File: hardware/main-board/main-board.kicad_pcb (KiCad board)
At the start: 4 copper layers, 100 x 100 mm, 154 parts, among them J1 BOOT, J10 8P8CDouble, J11 Qwiic, J12 Qwiic, J13 Qwiic, J14 Micro_SD_Card_Det, J15 Interrupts1, J16 Interrupts2, J17 Battery, J2 USB Header, J3 JTAG, J4 5V Input, J5 StatusPanel, J6 Qwiic, J7 8P8CDouble, J8 8P8CDouble, J9 8P8CDouble, Q1 N Channel, Q10 N Channel, Q11 N Channel, Q12 N Channel, Q13 P Channel, Q14 P Channel, Q15 P Channel, Q16 P Channel, Q17 P Channel, Q2 N Channel, Q3 N Channel, Q4 N Channel, Q5 P Channel, Q6 P Channel, Q7 P Channel, Q8 P Channel, Q9 N Channel, U1 STM32H743ZITx, U10 ISL83490, U11 ISL83490, U12 ISL83490, U2 USBLC6-2SC6, U3 3.3V Reg, U4 AP2120N-3.3TRG1 / XC6206P332MR, U5 ISL83490, U6 ISL83490, U7 ISL83490, U8 ISL83490, U9 ISL83490, X1 20MHz Oscillator, X2 32.768kHz Oscillator

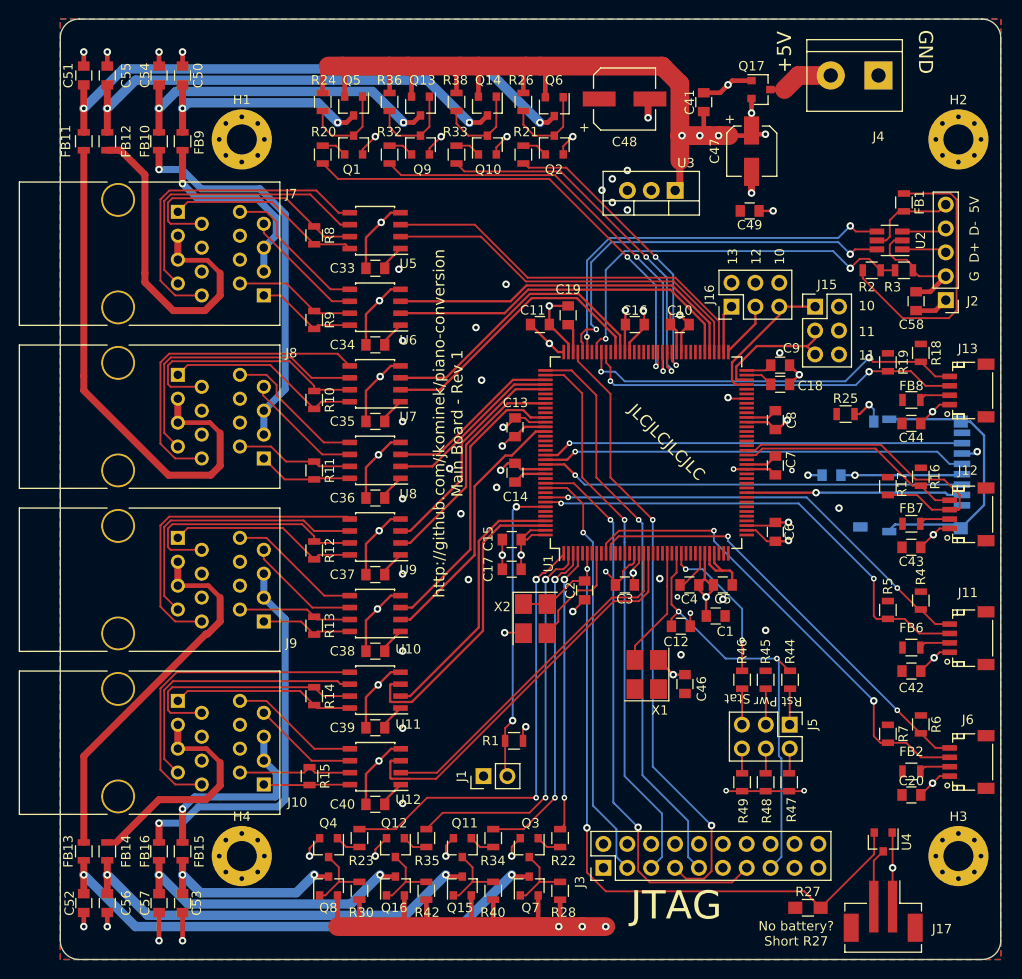
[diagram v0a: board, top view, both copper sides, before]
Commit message: main board changes for rev 2 per issue #41
* Added a bit more thermal relief to everything on the top layer
* Looked at the RS485 and I2C caps thermal relief and called it good enough.
* Fixed silkscreen of C20 and most everything else, as I upgraded to KiCad 6 footprints and the refs all moved.
* Changed the ferrite bead footprint to the handsoldering one.
* Tweaked the specified values for the Pwr and Stat LEDs, but not much.
* Removed battery connector and associated bits.
* That left remove to move over the JTAG header.
* Switched to using the SDMMC peripheral for accessing the SD card.
* Had SDCARD_DET net attached to the wrong side of the pull up; fixed.
* Made all of the high speed traces nice and filleted.
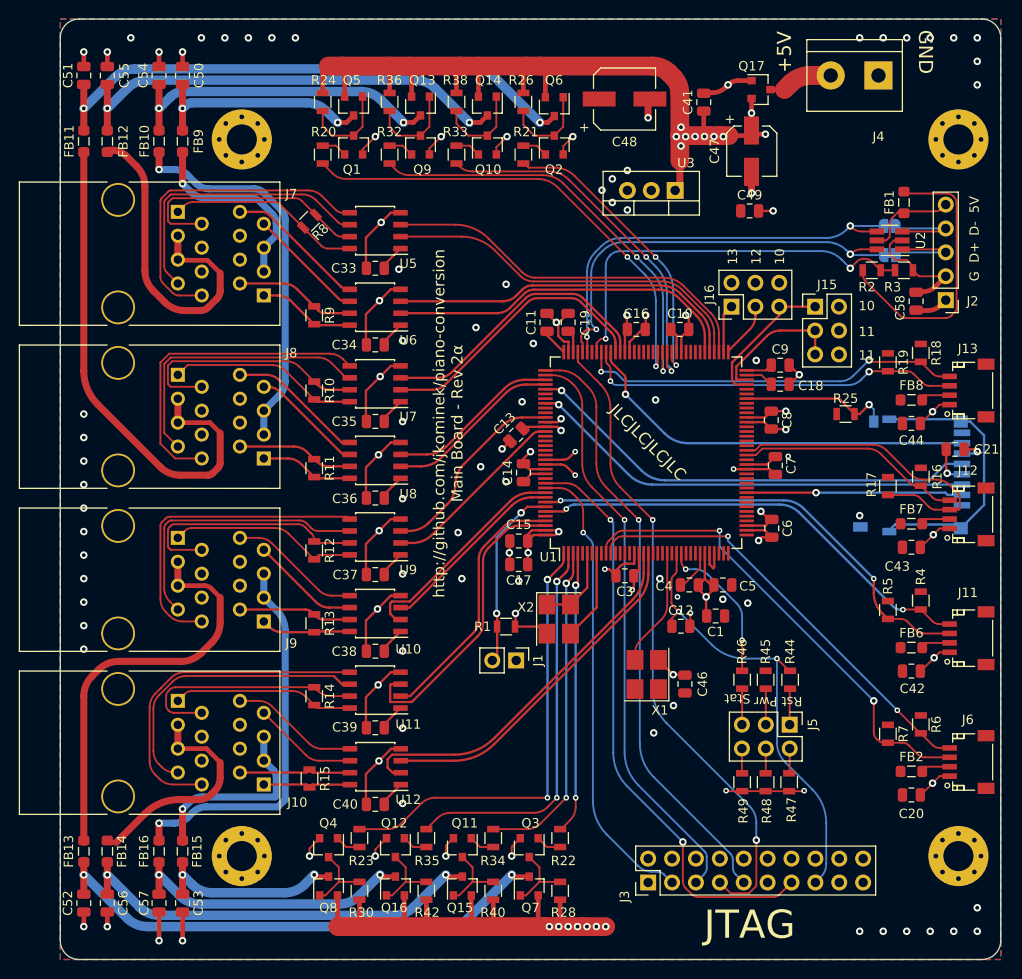
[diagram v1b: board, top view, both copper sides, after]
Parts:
- removed C2: DC6, Capacitors_SMD:C_0805
- removed J17: Battery, Connectors_JST:JST_PH_B2B-PH-SM4-TB_02x2.00mm_Straight
- removed R27: DNP, Resistors_SMD:R_0805_HandSoldering
- removed U4: AP2120N-3.3TRG1 / XC6206P332MR, TO_SOT_Packages_SMD:SOT-23
- added JP1: SolderJumper_2_Bridged, Jumper:SolderJumper-2_P1.3mm_Bridged_RoundedPad1.0x1.5mm, B.Cu at (183.2, 60.0)
- added JP2: SolderJumper_2_Bridged, Jumper:SolderJumper-2_P1.3mm_Bridged_RoundedPad1.0x1.5mm, B.Cu at (183.2, 63.1)
- C1, C10, C11, C12, C13, C14, C15, C16, C17, C18, C19, C20, C3, C33, C34, C35, C36, C37, C38, C39, C4, C40, C41, C42, C43, C44, C46, C49, C5, C50, C51, C52, C53, C54, C55, C56, C57, C58, C6, C7, C8, C9: footprint Capacitors_SMD:C_0805 -> Capacitor_SMD:C_0805_2012Metric
- C21: footprint Capacitors_SMD:C_0805 -> Capacitor_SMD:C_0805_2012Metric; moved to F.Cu
- FB1, FB10, FB11, FB12, FB13, FB14, FB15, FB16, FB2, FB6, FB7, FB8, FB9: footprint Inductors_SMD:L_0805 -> Inductor_SMD:L_0805_2012Metric_Pad1.05x1.20mm_HandSolder
- R48, R49: value 3300 -> 660
- moved C21 13.4 mm to (190.2, 83.8), turned to 180 degrees
- moved J1 12.8 mm to (143.5, 106.2), turned to -90 degrees
- moved R1 12.2 mm to (142.4, 102.6)
- moved J3 5.01 mm to (157.5, 129.8)
- moved X2 2.50 mm to (148.0, 101.8)
- moved R8 1.58 mm to (121.5, 59.5), turned to -135 degrees
- moved R10 1.00 mm to (122.0, 77.5)
- moved C3 0.97 mm to (155.0, 97.2)
- moved C17 0.90 mm to (143.8, 96.0)
- moved C14 0.90 mm to (144.2, 86.2)
- moved C13 0.82 mm to (143.5, 82.2), turned to -135 degrees
- moved C11 0.79 mm to (146.8, 70.2), turned to 90 degrees
- moved C15 0.77 mm to (143.8, 93.5)
- moved C19 0.75 mm to (149.0, 70.2)
- moved C6 0.54 mm to (170.7, 92.2)
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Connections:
- J14 pad 1: (no net) -> unconnected-(J14-Pad1)
- J14 pad 11: Net-(J14-Pad11) -> unconnected-(J14-Pad11)
- J14 pad 3: /SPI6_MOSI -> /SDMMC1_CMD
- J14 pad 5: /SPI6_SCK -> /SDMMC1_CK
- J14 pad 7: /SPI6_MISO -> /SDMMC1_D0
- J14 pad 8: (no net) -> unconnected-(J14-Pad8)
- J14 pad 9: Net-(J14-Pad9) -> /SDCARD_DET
- J3 pad 11: (no net) -> unconnected-(J3-Pad11)
- J3 pad 17: (no net) -> unconnected-(J3-Pad17)
- J3 pad 19: (no net) -> unconnected-(J3-Pad19)
- R25 pad 2: Net-(J14-Pad9) -> /SDCARD_DET
- U1 pad 102: (no net) -> unconnected-(U1-Pad102)
- U1 pad 113: /UART5_TX -> /SDMMC1_CK
- U1 pad 114: (no net) -> unconnected-(U1-Pad114)
- U1 pad 115: (no net) -> unconnected-(U1-Pad115)
- U1 pad 116: /UART5_RX -> /SDMMC1_CMD
- U1 pad 117: (no net) -> unconnected-(U1-Pad117)
- U1 pad 118: (no net) -> unconnected-(U1-Pad118)
- U1 pad 12: (no net) -> unconnected-(U1-Pad12)
- U1 pad 123: (no net) -> unconnected-(U1-Pad123)
- U1 pad 124: (no net) -> unconnected-(U1-Pad124)
- U1 pad 125: (no net) -> unconnected-(U1-Pad125)
- U1 pad 126: (no net) -> unconnected-(U1-Pad126)
- U1 pad 127: /SPI6_MISO -> unconnected-(U1-Pad127)
- U1 pad 128: /SPI6_SCK -> unconnected-(U1-Pad128)
- U1 pad 129: /SPI6_MOSI -> unconnected-(U1-Pad129)
- U1 pad 13: (no net) -> unconnected-(U1-Pad13)
- U1 pad 132: (no net) -> unconnected-(U1-Pad132)
- U1 pad 135: (no net) -> /UART5_RX
- U1 pad 136: /I2C1_SCL -> /UART5_TX
- U1 pad 139: (no net) -> /I2C1_SCL
- U1 pad 14: (no net) -> unconnected-(U1-Pad14)
- U1 pad 140: (no net) -> unconnected-(U1-Pad140)
- U1 pad 15: (no net) -> unconnected-(U1-Pad15)
- U1 pad 20: (no net) -> unconnected-(U1-Pad20)
- U1 pad 21: (no net) -> unconnected-(U1-Pad21)
- U1 pad 22: (no net) -> unconnected-(U1-Pad22)
- U1 pad 24: (no net) -> unconnected-(U1-Pad24)
- U1 pad 27: (no net) -> unconnected-(U1-Pad27)
- U1 pad 28: (no net) -> unconnected-(U1-Pad28)
- U1 pad 29: (no net) -> unconnected-(U1-Pad29)
- U1 pad 34: (no net) -> unconnected-(U1-Pad34)
- U1 pad 35: (no net) -> unconnected-(U1-Pad35)
- U1 pad 36: (no net) -> unconnected-(U1-Pad36)
- U1 pad 37: (no net) -> unconnected-(U1-Pad37)
- U1 pad 40: (no net) -> unconnected-(U1-Pad40)
- U1 pad 41: (no net) -> unconnected-(U1-Pad41)
- U1 pad 42: (no net) -> unconnected-(U1-Pad42)
- U1 pad 43: (no net) -> unconnected-(U1-Pad43)
- U1 pad 44: (no net) -> unconnected-(U1-Pad44)
- U1 pad 45: (no net) -> unconnected-(U1-Pad45)
- U1 pad 47: (no net) -> unconnected-(U1-Pad47)
- U1 pad 48: (no net) -> unconnected-(U1-Pad48)
- U1 pad 49: (no net) -> unconnected-(U1-Pad49)
- U1 pad 5: (no net) -> unconnected-(U1-Pad5)
- U1 pad 50: (no net) -> unconnected-(U1-Pad50)
- U1 pad 53: (no net) -> unconnected-(U1-Pad53)
- U1 pad 56: (no net) -> unconnected-(U1-Pad56)
- U1 pad 57: (no net) -> unconnected-(U1-Pad57)
- U1 pad 58: (no net) -> unconnected-(U1-Pad58)
- U1 pad 59: (no net) -> unconnected-(U1-Pad59)
- U1 pad 6: +BATT -> +3V3
- U1 pad 60: (no net) -> unconnected-(U1-Pad60)
- U1 pad 63: (no net) -> unconnected-(U1-Pad63)
- U1 pad 64: (no net) -> unconnected-(U1-Pad64)
- U1 pad 65: (no net) -> unconnected-(U1-Pad65)
- U1 pad 66: GND -> /SDCARD_DET
- U1 pad 67: (no net) -> unconnected-(U1-Pad67)
- U1 pad 68: (no net) -> unconnected-(U1-Pad68)
- U1 pad 7: (no net) -> unconnected-(U1-Pad7)
- U1 pad 79: (no net) -> unconnected-(U1-Pad79)
- U1 pad 80: (no net) -> unconnected-(U1-Pad80)
- U1 pad 81: (no net) -> unconnected-(U1-Pad81)
- U1 pad 82: (no net) -> unconnected-(U1-Pad82)
- U1 pad 89: (no net) -> unconnected-(U1-Pad89)
- U1 pad 9: (no net) -> unconnected-(U1-Pad9)
- U1 pad 90: (no net) -> unconnected-(U1-Pad90)
- U1 pad 91: (no net) -> unconnected-(U1-Pad91)
- U1 pad 92: (no net) -> unconnected-(U1-Pad92)
- U1 pad 93: (no net) -> unconnected-(U1-Pad93)
- U1 pad 98: (no net) -> /SDMMC1_D0
- U10 pad 2: /USART2_RX -> /UART5_RX
- U10 pad 3: /USART2_TX -> /UART5_TX
- U9 pad 2: /UART5_RX -> /USART2_RX
- U9 pad 3: /UART5_TX -> /USART2_TX
- X2 pad 1: +BATT -> +3V3
- X2 pad 4: +BATT -> +3V3
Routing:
- net +BATT: track 79.6 -> 0.00 mm, vias 2 -> 0
- net /SDMMC1_CK: track 0.00 -> 48.9 mm, vias 0 -> 1
- net /SDMMC1_CMD: track 0.00 -> 47.7 mm, vias 0 -> 1
- net /SPI6_SCK: track 45.2 -> 0.00 mm, vias 1 -> 0
- net /SPI6_MOSI: track 45.2 -> 0.00 mm, vias 1 -> 0
- net /SPI6_MISO: track 44.8 -> 0.00 mm, vias 1 -> 0
- net /SDMMC1_D0: track 0.00 -> 42.9 mm, vias 0 -> 1
- net Net-(J14-Pad11): track 29.9 -> 0.00 mm
- net unconnected-(J14-Pad11): track 0.00 -> 29.9 mm
- net GND: track 237.4 -> 217.6 mm, vias 56 -> 86
- net /SDCARD_DET: track 0.00 -> 16.1 mm, vias 0 -> 1
- net Net-(J1-Pad2): track 32.3 -> 19.9 mm
- net /USART2_TX: track 30.8 -> 21.3 mm
- net /USART2_RX: track 28.0 -> 20.1 mm
- net +3V3: track 97.1 -> 90.2 mm, vias 34 -> 37
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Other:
- net class Default removed
- board text added: "http://github.com/jkominek/piano-conversion Main Board - Rev 2α"
- board text removed: "No battery? Short R27"
- board text removed: "http://github.com/jkominek/piano-conversion Main Board - Rev 1"

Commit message: Convert all other mounting holes to non-pad variety.
Reroute a few traces to be shorter.
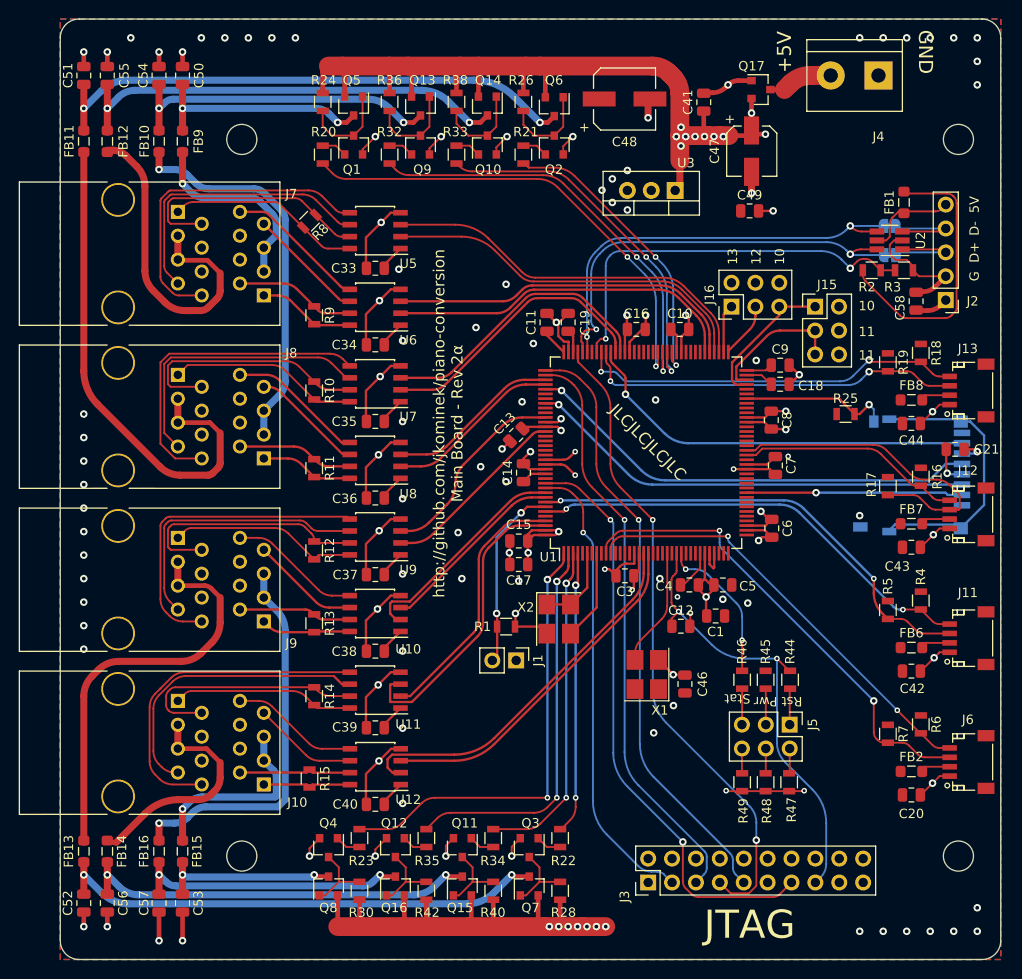
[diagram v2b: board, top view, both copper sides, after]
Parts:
- H1, H2, H3, H4: footprint Mounting_Holes:MountingHole_3.2mm_M3_Pad_Via -> MountingHole:MountingHole_3.2mm_M3
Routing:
- net Net-(C52-Pad1): track 55.3 -> 53.1 mm
- net Net-(C56-Pad1): track 44.7 -> 42.8 mm
- net Net-(C57-Pad1): track 31.0 -> 29.6 mm
- net Net-(C51-Pad1): track 59.2 -> 58.0 mm
- net Net-(C53-Pad1): track 20.4 -> 19.3 mm
- net Net-(C55-Pad1): track 48.6 -> 47.7 mm
- net Net-(C54-Pad1): track 35.0 -> 34.4 mm

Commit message: Next revs of the important boards
Includes some tiny DRC tweaks for the LED power board.
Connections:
- net Net-(Q1-Pad3) renamed /Power/PWR2_PG
- net Net-(Q10-Pad3) renamed /Power/PWR1_PG
- net Net-(Q11-Pad3) renamed /Power/PWR7_PG
- net Net-(Q12-Pad3) renamed /Power/PWR6_PG
- net Net-(Q13-Pad1) renamed /Power/PWR4_PG
- net Net-(Q2-Pad3) renamed /Power/PWR3_PG
- net Net-(Q3-Pad3) renamed /Power/PWR5_PG
- net Net-(Q4-Pad3) renamed /Power/PWR8_PG
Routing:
- net GND: track 217.6 -> 211.9 mm, vias 86 -> 96
- net PWR5: track 44.3 -> 39.9 mm
- net /USART6_RX: track 29.9 -> 28.9 mm
- net /USART6_TX: track 30.3 -> 29.4 mm
- net /LINK7_Z: track 31.3 -> 30.4 mm
- net /LINK7_Y: track 35.7 -> 34.9 mm
- net /USART3_RX: track 37.4 -> 36.7 mm
- net /USART3_TX: track 37.9 -> 37.2 mm
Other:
- board text added: "Thermal relief"
- board text added: "http://github.com/jkominek/piano-conversion Main Board - Rev 2"
- board text removed: "http://github.com/jkominek/piano-conversion Main Board - Rev 2α"
